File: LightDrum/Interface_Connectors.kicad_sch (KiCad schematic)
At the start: 6 parts, among them J6 0525593652, J7 0541323662, J8 PWR-CONN

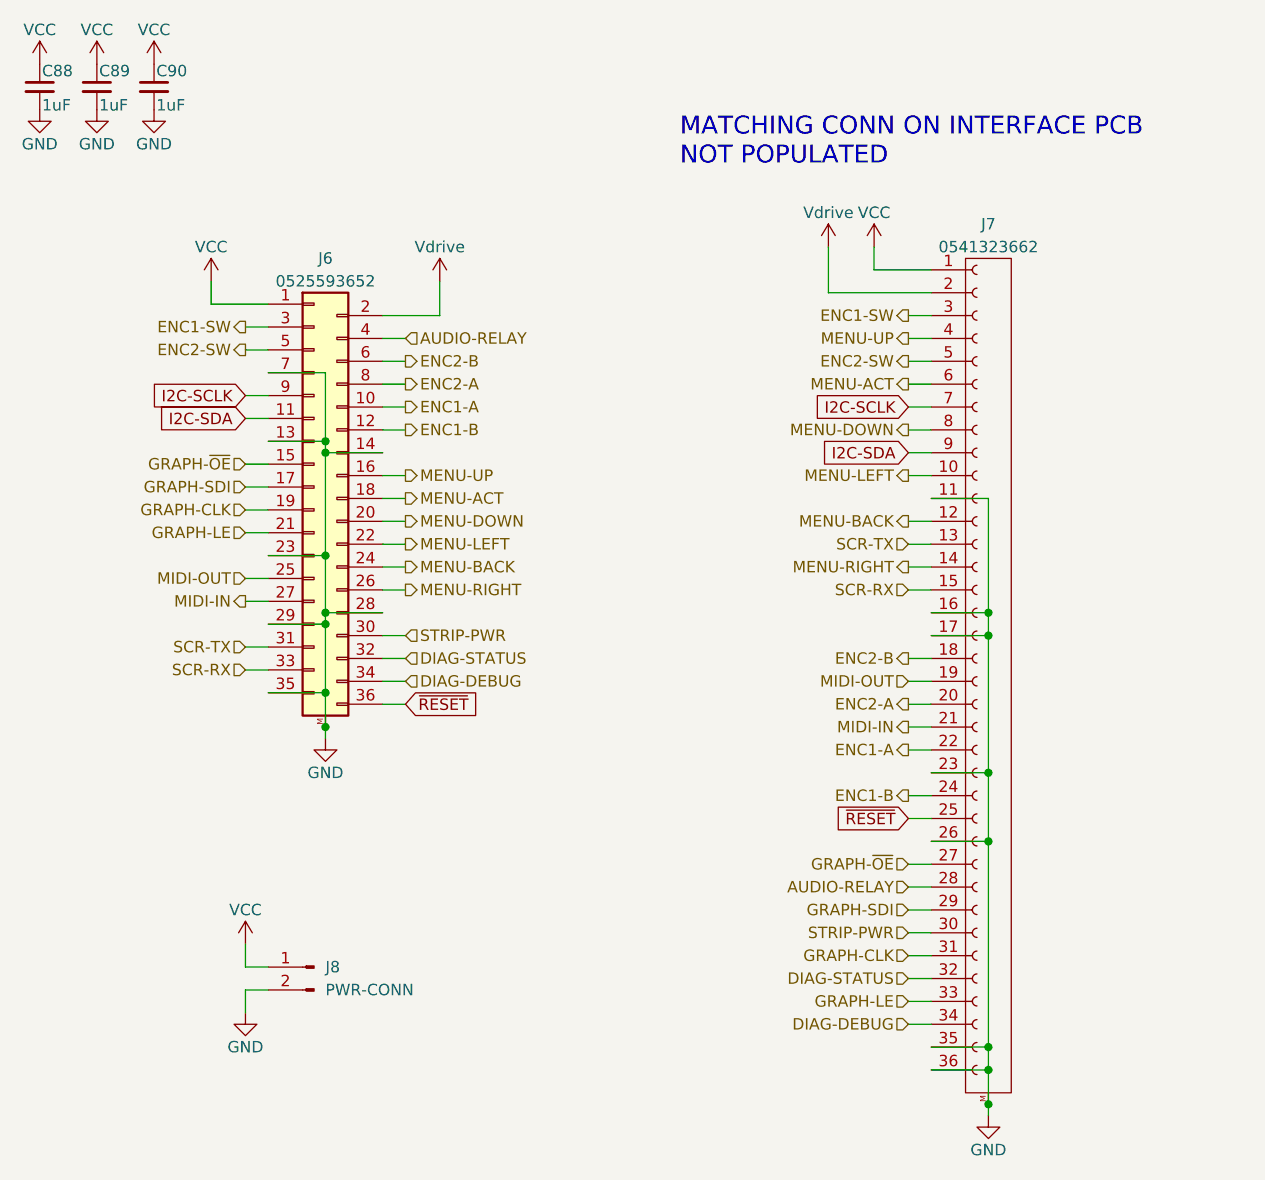
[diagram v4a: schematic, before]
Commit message: Replaced display and FPC cable
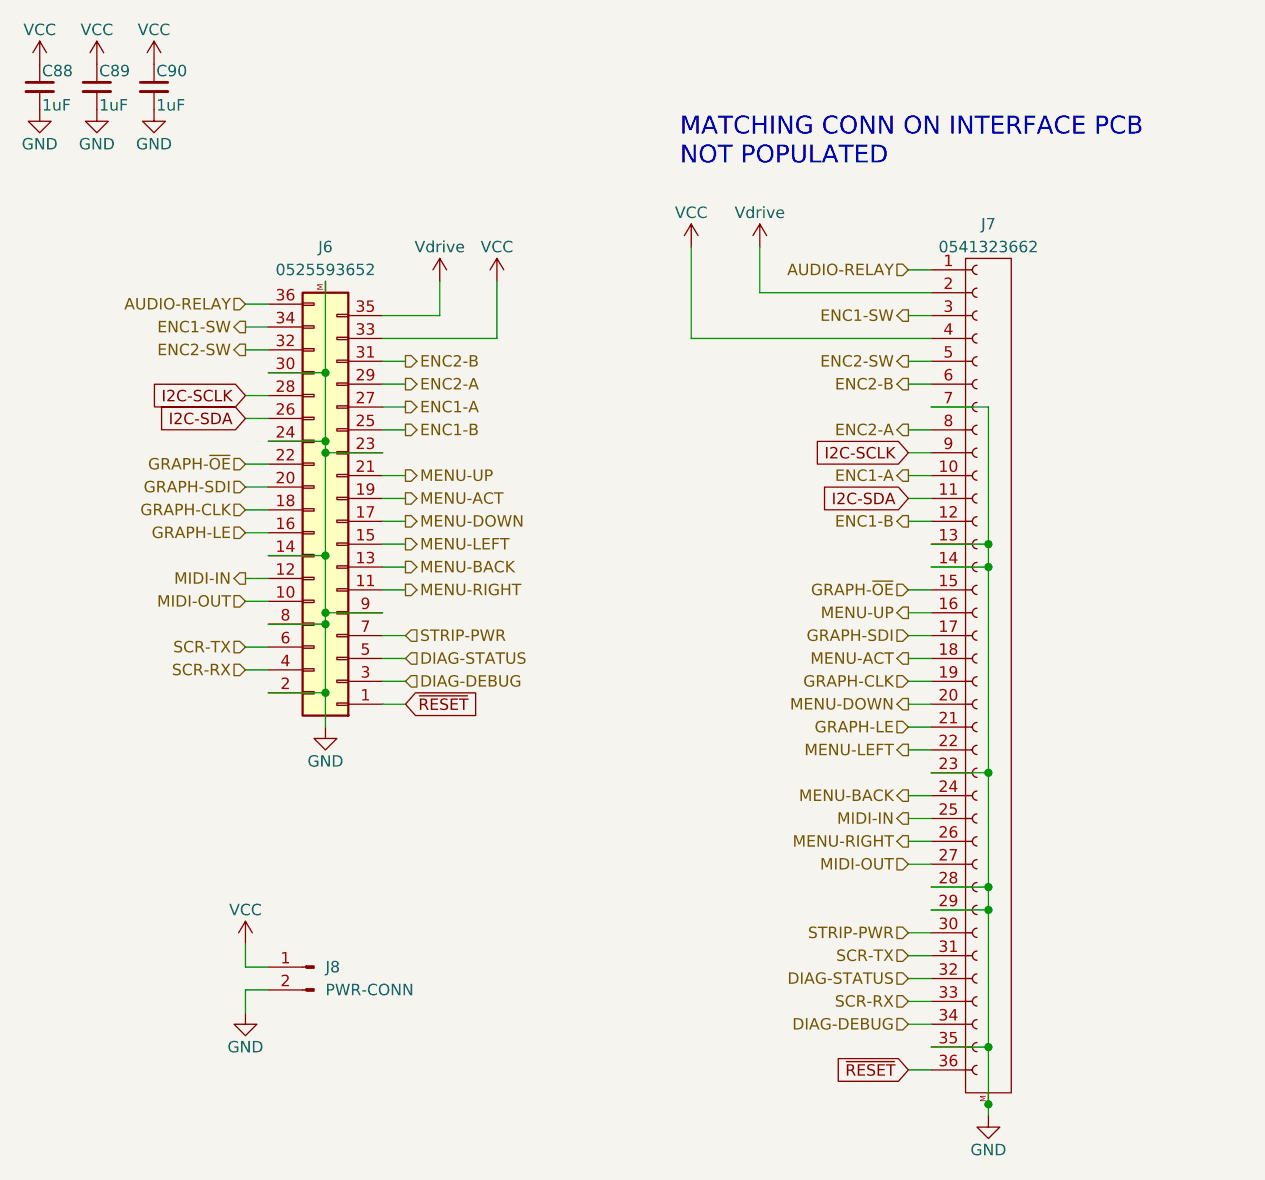
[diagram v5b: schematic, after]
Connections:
- net AUDIO-RELAY: now also J6.36 (Pin_36), J7.1 (Pin_1); no longer J6.4 (Pin_4), J7.28 (Pin_28)
- net DIAG-DEBUG: now also J6.3 (Pin_3); no longer J6.34 (Pin_34)
- net DIAG-STATUS: now also J6.5 (Pin_5); no longer J6.32 (Pin_32)
- net ENC1-A: now also J6.27 (Pin_27), J7.10 (Pin_10); no longer J6.10 (Pin_10), J7.22 (Pin_22)
- net ENC1-B: now also J6.25 (Pin_25), J7.12 (Pin_12); no longer J6.12 (Pin_12), J7.24 (Pin_24)
- net ENC1-SW: now also J6.34 (Pin_34); no longer J6.3 (Pin_3)
- net ENC2-A: now also J6.29 (Pin_29), J7.8 (Pin_8); no longer J6.8 (Pin_8), J7.20 (Pin_20)
- net ENC2-B: now also J6.31 (Pin_31), J7.6 (Pin_6); no longer J6.6 (Pin_6), J7.18 (Pin_18)
- net ENC2-SW: now also J6.32 (Pin_32); no longer J6.5 (Pin_5)
- net GND: now also J6.2 (Pin_2), J6.24 (Pin_24), J6.30 (Pin_30), J6.8 (Pin_8), J6.9 (Pin_9), J7.13 (Pin_13), J7.14 (Pin_14), J7.28 (Pin_28), J7.29 (Pin_29), J7.7 (Pin_7); no longer J6.13 (Pin_13), J6.28 (Pin_28), J6.29 (Pin_29), J6.35 (Pin_35), J6.7 (Pin_7), J7.11 (Pin_11), J7.16 (Pin_16), J7.17 (Pin_17), J7.26 (Pin_26), J7.36 (Pin_36)
- net GRAPH-CLK: now also J6.18 (Pin_18), J7.19 (Pin_19); no longer J6.19 (Pin_19), J7.31 (Pin_31)
- net GRAPH-LE: now also J6.16 (Pin_16), J7.21 (Pin_21); no longer J6.21 (Pin_21), J7.33 (Pin_33)
- net GRAPH-SDI: now also J6.20 (Pin_20), J7.17 (Pin_17); no longer J6.17 (Pin_17), J7.29 (Pin_29)
- net GRAPH-~{OE}: now also J6.22 (Pin_22), J7.15 (Pin_15); no longer J6.15 (Pin_15), J7.27 (Pin_27)
- net I2C-SCLK: now also J6.28 (Pin_28), J7.9 (Pin_9); no longer J6.9 (Pin_9), J7.7 (Pin_7)
- net I2C-SDA: now also J6.26 (Pin_26), J7.11 (Pin_11); no longer J6.11 (Pin_11), J7.9 (Pin_9)
- net MENU-ACT: now also J6.19 (Pin_19), J7.18 (Pin_18); no longer J6.18 (Pin_18), J7.6 (Pin_6)
- net MENU-BACK: now also J6.13 (Pin_13), J7.24 (Pin_24); no longer J6.24 (Pin_24), J7.12 (Pin_12)
- net MENU-DOWN: now also J6.17 (Pin_17), J7.20 (Pin_20); no longer J6.20 (Pin_20), J7.8 (Pin_8)
- net MENU-LEFT: now also J6.15 (Pin_15), J7.22 (Pin_22); no longer J6.22 (Pin_22), J7.10 (Pin_10)
- net MENU-RIGHT: now also J6.11 (Pin_11), J7.26 (Pin_26); no longer J6.26 (Pin_26), J7.14 (Pin_14)
- net MENU-UP: now also J6.21 (Pin_21), J7.16 (Pin_16); no longer J6.16 (Pin_16), J7.4 (Pin_4)
- net MIDI-IN: now also J6.12 (Pin_12), J7.25 (Pin_25); no longer J6.27 (Pin_27), J7.21 (Pin_21)
- net MIDI-OUT: now also J6.10 (Pin_10), J7.27 (Pin_27); no longer J6.25 (Pin_25), J7.19 (Pin_19)
- net SCR-RX: now also J6.4 (Pin_4), J7.33 (Pin_33); no longer J6.33 (Pin_33), J7.15 (Pin_15)
- net SCR-TX: now also J6.6 (Pin_6), J7.31 (Pin_31); no longer J6.31 (Pin_31), J7.13 (Pin_13)
- net STRIP-PWR: now also J6.7 (Pin_7); no longer J6.30 (Pin_30)
- net VCC: now also J6.33 (Pin_33), J7.4 (Pin_4); no longer J6.1 (Pin_1), J7.1 (Pin_1)
- net Vdrive: now also J6.35 (Pin_35); no longer J6.2 (Pin_2)
- net ~{RESET}: now also J6.1 (Pin_1), J7.36 (Pin_36); no longer J6.36 (Pin_36), J7.25 (Pin_25)
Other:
- moved on the sheet: J6

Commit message: First pass over schematic (WIP)
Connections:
- net GND: no longer J6.2 (Pin_2), J7.35 (Pin_35)
- new net VDD: J6.2 (Pin_2), J7.35 (Pin_35)
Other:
- moved on the sheet: J8
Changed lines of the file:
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@@
   (title_block
     (title "LightDrum")
-    (rev "REV7")
+    (rev "REV8")
     (company "Daxxn Industries")
   )
-  (junction (at 50.8 90.17) (diameter 0) (color 0 0 0 0)
-  )
   (junction (at 124.46 76.2) (diameter 0) (color 0 0 0 0)
   )
@@
   (junction (at 50.8 62.23) (diameter 0) (color 0 0 0 0)
   )
-  (junction (at 124.46 129.54) (diameter 0) (color 0 0 0 0)
-  )
   (junction (at 50.8 54.61) (diameter 0) (color 0 0 0 0)
   )
@@
     (stroke (width 0) (type default) (color 0 0 0 0))
   )
-  (wire (pts (xy 44.45 120.65) (xy 41.91 120.65))
+  (wire (pts (xy 52.07 110.49) (xy 50.8 110.49))
     (stroke (width 0) (type default) (color 0 0 0 0))
   )
@@
     (stroke (width 0) (type default) (color 0 0 0 0))
   )
-  (wire (pts (xy 124.46 114.3) (xy 124.46 129.54))
-    (stroke (width 0) (type default) (color 0 0 0 0))
-  )
-  (wire (pts (xy 50.8 90.17) (xy 50.8 93.98))
+  (wire (pts (xy 124.46 114.3) (xy 124.46 135.89))
     (stroke (width 0) (type default) (color 0 0 0 0))
   )
@@
     (stroke (width 0) (type default) (color 0 0 0 0))
   )
-  (wire (pts (xy 115.57 132.08) (xy 118.11 132.08))
+  (wire (pts (xy 106.68 132.08) (xy 118.11 132.08))
     (stroke (width 0) (type default) (color 0 0 0 0))
   )
@@
     (stroke (width 0) (type default) (color 0 0 0 0))
   )
+  (wire (pts (xy 29.21 88.9) (xy 29.21 90.17))
+    (stroke (width 0) (type default) (color 0 0 0 0))
+  )
   (wire (pts (xy 91.44 40.64) (xy 91.44 50.8))
     (stroke (width 0) (type default) (color 0 0 0 0))
@@
     (stroke (width 0) (type default) (color 0 0 0 0))
   )
-  (wire (pts (xy 44.45 90.17) (xy 50.8 90.17))
-    (stroke (width 0) (type default) (color 0 0 0 0))
-  )
   (wire (pts (xy 69.85 50.8) (xy 57.15 50.8))
     (stroke (width 0) (type default) (color 0 0 0 0))
@@
     (stroke (width 0) (type default) (color 0 0 0 0))
   )
+  (wire (pts (xy 29.21 90.17) (xy 44.45 90.17))
+    (stroke (width 0) (type default) (color 0 0 0 0))
+  )
   (wire (pts (xy 118.11 121.92) (xy 115.57 121.92))
     (stroke (width 0) (type default) (color 0 0 0 0))
   )
-  (wire (pts (xy 50.8 82.55) (xy 50.8 90.17))
+  (wire (pts (xy 97.79 129.54) (xy 118.11 129.54))
+    (stroke (width 0) (type default) (color 0 0 0 0))
+  )
+  (wire (pts (xy 50.8 82.55) (xy 50.8 93.98))
     (stroke (width 0) (type default) (color 0 0 0 0))
   )
@@
     (stroke (width 0) (type default) (color 0 0 0 0))
   )
+  (wire (pts (xy 97.79 128.27) (xy 97.79 129.54))
+    (stroke (width 0) (type default) (color 0 0 0 0))
+  )
   (wire (pts (xy 91.44 50.8) (xy 118.11 50.8))
     (stroke (width 0) (type default) (color 0 0 0 0))
@@
     (stroke (width 0) (type default) (color 0 0 0 0))
   )
-  (wire (pts (xy 41.91 120.65) (xy 41.91 118.11))
+  (wire (pts (xy 50.8 110.49) (xy 50.8 109.22))
     (stroke (width 0) (type default) (color 0 0 0 0))
   )
@@
     (stroke (width 0) (type default) (color 0 0 0 0))
   )
-  (wire (pts (xy 118.11 129.54) (xy 124.46 129.54))
-    (stroke (width 0) (type default) (color 0 0 0 0))
-  )
   (wire (pts (xy 63.5 48.26) (xy 63.5 44.45))
     (stroke (width 0) (type default) (color 0 0 0 0))
@@
     (stroke (width 0) (type default) (color 0 0 0 0))
   )
-  (wire (pts (xy 44.45 123.19) (xy 41.91 123.19))
+  (wire (pts (xy 52.07 113.03) (xy 50.8 113.03))
     (stroke (width 0) (type default) (color 0 0 0 0))
   )
@@
     (stroke (width 0) (type default) (color 0 0 0 0))
   )
-  (wire (pts (xy 41.91 123.19) (xy 41.91 125.73))
+  (wire (pts (xy 50.8 113.03) (xy 50.8 114.3))
     (stroke (width 0) (type default) (color 0 0 0 0))
   )
@@
   )
   (wire (pts (xy 118.11 91.44) (xy 115.57 91.44))
-    (stroke (width 0) (type default) (color 0 0 0 0))
-  )
-  (wire (pts (xy 124.46 129.54) (xy 124.46 135.89))
     (stroke (width 0) (type default) (color 0 0 0 0))
   )
@@
     )
   )
-  (global_label "~{RESET}" (shape input) (at 115.57 132.08 180) (fields_autoplaced)
-    (effects (font (size 1.27 1.27)) (justify right))
-    (property "Intersheet References" "${INTERSHEET_REFS}" (id 0) (at 107.4117 132.0006 0)
+  (global_label "~{RESET}" (shape input) (at 106.68 132.08 180) (fields_autoplaced)
+    (effects (font (size 1.27 1.27)) (justify right))
+    (property "Intersheet References" "${INTERSHEET_REFS}" (id 0) (at 98.5217 132.0006 0)
       (effects (font (size 1.27 1.27)) (justify right) hide)
     )
@@
     (pin "1")
   )
-  (symbol (lib_id "power:GND") (at 41.91 125.73 0) (unit 1)
-    (in_bom yes) (on_board yes)
-    (property "Reference" "#PWR0135" (id 0) (at 41.91 132.08 0)
-      (effects (font (size 1.27 1.27)) hide)
-    )
-    (property "Value" "GND" (id 1) (at 41.91 129.54 0))
-    (property "Footprint" "" (id 2) (at 41.91 125.73 0)
-      (effects (font (size 1.27 1.27)) hide)
-    )
-    (property "Datasheet" "" (id 3) (at 41.91 125.73 0)
+  (symbol (lib_id "power:GND") (at 50.8 114.3 0) (unit 1)
+    (in_bom yes) (on_board yes)
+    (property "Reference" "#PWR0135" (id 0) (at 50.8 120.65 0)
+      (effects (font (size 1.27 1.27)) hide)
+    )
+    (property "Value" "GND" (id 1) (at 50.8 118.11 0))
+    (property "Footprint" "" (id 2) (at 50.8 114.3 0)
+      (effects (font (size 1.27 1.27)) hide)
+    )
+    (property "Datasheet" "" (id 3) (at 50.8 114.3 0)
       (effects (font (size 1.27 1.27)) hide)
     )
@@
     (pin "1")
   )
+  (symbol (lib_id "power:VDD") (at 97.79 128.27 0) (unit 1)
+    (in_bom yes) (on_board yes)
+    (property "Reference" "#PWR069" (id 0) (at 97.79 132.08 0)
+      (effects (font (size 1.27 1.27)) hide)
+    )
+    (property "Value" "VDD" (id 1) (at 97.79 124.46 0))
+    (property "Footprint" "" (id 2) (at 97.79 128.27 0)
+      (effects (font (size 1.27 1.27)) hide)
+    )
+    (property "Datasheet" "" (id 3) (at 97.79 128.27 0)
+      (effects (font (size 1.27 1.27)) hide)
+    )
+    (pin "1")
+  )
   (symbol (lib_id "power:Vdrive") (at 63.5 44.45 0) (unit 1)
     (in_bom yes) (on_board yes)
@@
     (pin "1")
   )
-  (symbol (lib_id "Connector:Conn_01x02_Male") (at 49.53 120.65 0) (mirror y) (unit 1)
-    (in_bom yes) (on_board yes)
-    (property "Reference" "J8" (id 0) (at 50.8 120.65 0)
+  (symbol (lib_id "Connector:Conn_01x02_Male") (at 57.15 110.49 0) (mirror y) (unit 1)
+    (in_bom yes) (on_board yes)
+    (property "Reference" "J8" (id 0) (at 58.42 110.49 0)
       (effects (font (size 1.27 1.27)) (justify right))
     )
-    (property "Value" "PWR-CONN" (id 1) (at 50.8 123.19 0)
+    (property "Value" "PWR-CONN" (id 1) (at 58.42 113.03 0)
       (effects (font (size 1.27 1.27)) (justify right))
     )
-    (property "Footprint" "Connector_JST:JST_XA_B02B-XASK-1_1x02_P2.50mm_Vertical" (id 2) (at 49.53 120.65 0)
-      (effects (font (size 1.27 1.27)) hide)
-    )
-    (property "Datasheet" "~" (id 3) (at 49.53 120.65 0)
+    (property "Footprint" "Connector_JST:JST_XA_B02B-XASK-1_1x02_P2.50mm_Vertical" (id 2) (at 57.15 110.49 0)
+      (effects (font (size 1.27 1.27)) hide)
+    )
+    (property "Datasheet" "~" (id 3) (at 57.15 110.49 0)
       (effects (font (size 1.27 1.27)) hide)
     )
     (pin "1")
     (pin "2")
+  )
+  (symbol (lib_id "power:VDD") (at 29.21 88.9 0) (unit 1)
+    (in_bom yes) (on_board yes)
+    (property "Reference" "#PWR068" (id 0) (at 29.21 92.71 0)
+      (effects (font (size 1.27 1.27)) hide)
+    )
+    (property "Value" "VDD" (id 1) (at 29.21 85.09 0))
+    (property "Footprint" "" (id 2) (at 29.21 88.9 0)
+      (effects (font (size 1.27 1.27)) hide)
+    )
+    (property "Datasheet" "" (id 3) (at 29.21 88.9 0)
+      (effects (font (size 1.27 1.27)) hide)
+    )
+    (pin "1")
   )
   (symbol (lib_id "power:GND") (at 19.05 25.4 0) (unit 1)
@@
     (pin "1")
   )
-  (symbol (lib_id "power:VCC") (at 41.91 118.11 0) (unit 1)
-    (in_bom yes) (on_board yes)
-    (property "Reference" "#PWR0136" (id 0) (at 41.91 121.92 0)
-      (effects (font (size 1.27 1.27)) hide)
-    )
-    (property "Value" "VCC" (id 1) (at 41.91 114.3 0))
-    (property "Footprint" "" (id 2) (at 41.91 118.11 0)
-      (effects (font (size 1.27 1.27)) hide)
-    )
-    (property "Datasheet" "" (id 3) (at 41.91 118.11 0)
-      (effects (font (size 1.27 1.27)) hide)
-    )
+  (symbol (lib_id "power:VCC") (at 50.8 109.22 0) (unit 1)
+    (in_bom yes) (on_board yes)
+    (property "Reference" "#PWR0136" (id 0) (at 50.8 113.03 0)
+      (effects (font (size 1.27 1.27)) hide)
+    )
+    (property "Value" "VCC" (id 1) (at 50.8 105.41 0))
+    (property "Footprint" "" (id 2) (at 50.8 109.22 0)
+      (effects (font (size 1.27 1.27)) hide)
+    )
+    (property "Datasheet" "" (id 3) (at 50.8 109.22 0)
+      (effects (font (size 1.27 1.27)) hide)
+    )
